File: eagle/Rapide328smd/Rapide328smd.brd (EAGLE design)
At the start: 50 x 50 mm, 34 parts, among them IC1 MEGA8-AI, J1 AVR_SPI_PRG_6PTH

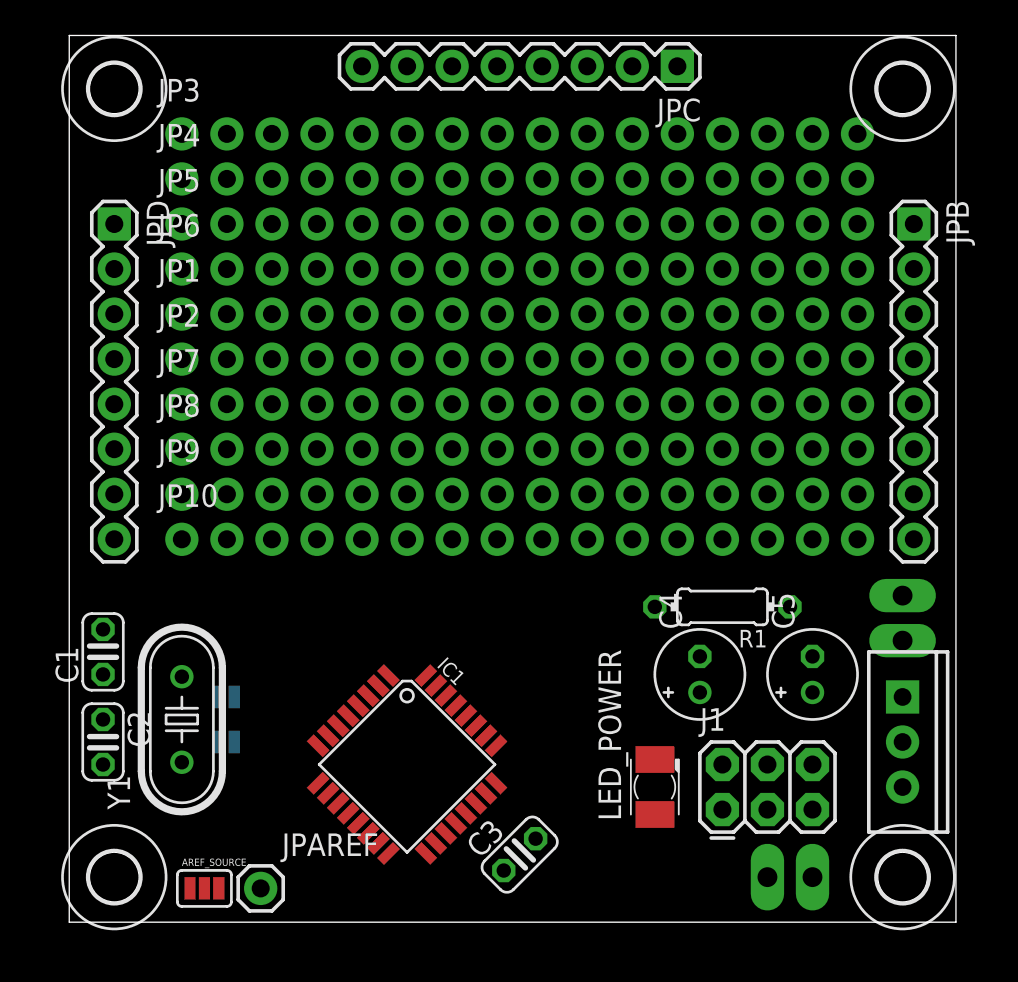
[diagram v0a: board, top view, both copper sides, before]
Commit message: Work in progress, started the wiring
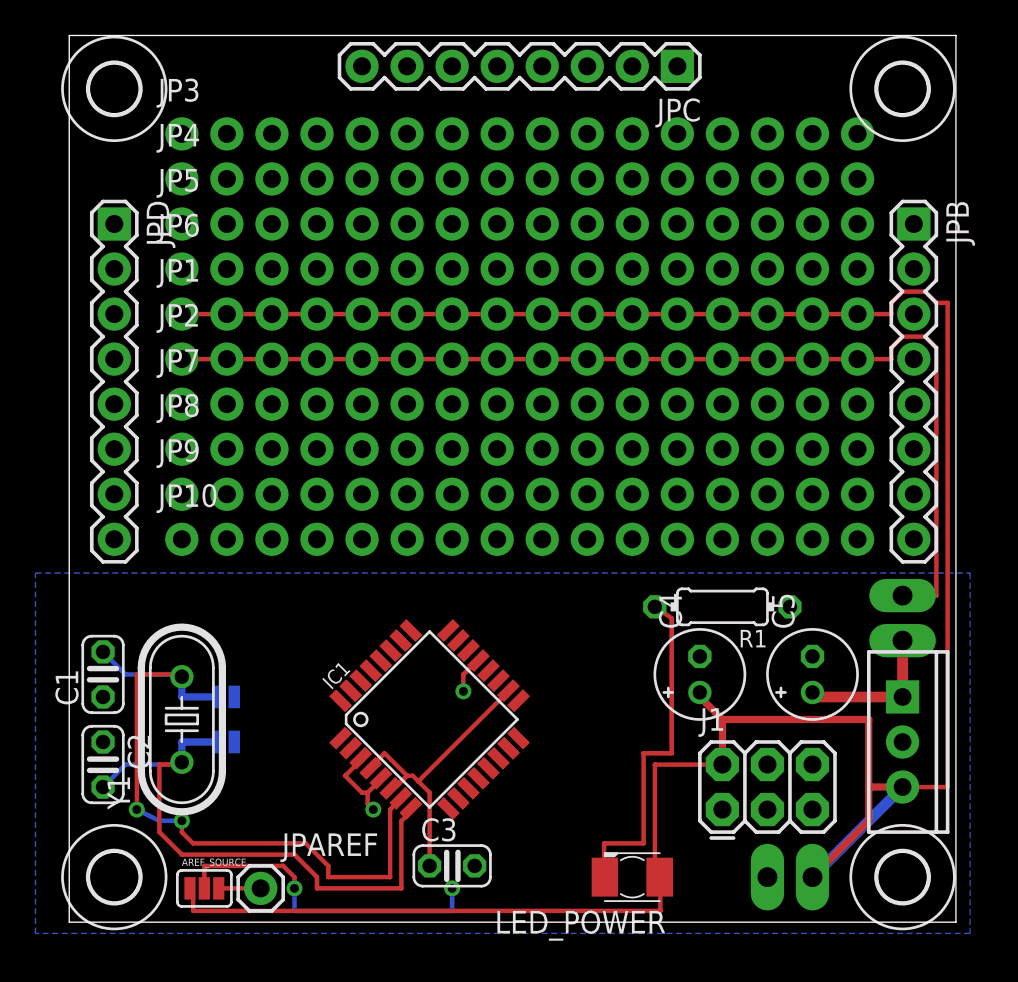
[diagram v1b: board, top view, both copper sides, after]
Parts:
- moved JP_RAW 17.6 mm to (47.0, 18.4), turned to 270 degrees
- moved JP_POWER 15.4 mm to (39.4, 2.54), turned to 0 degrees
- moved LED_POWER 5.24 mm to (31.8, 2.54), turned to 180 degrees
- moved C3 3.86 mm to (21.6, 3.17), turned to 0 degrees
- moved IC1 2.84 mm to (20.3, 11.4), turned to 45 degrees
- moved C1 1.27 mm to (1.91, 14.0)
- moved C2 1.27 mm to (1.91, 8.89)
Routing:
- net VCC: track 0.00 -> 133.1 mm
- net GND: track 0.00 -> 66.9 mm, vias 0 -> 2
- net N$25: track 0.00 -> 31.4 mm, vias 0 -> 2
- net N$34: track 0.00 -> 29.5 mm
- net N$2: track 0.00 -> 25.1 mm
- net N$30: track 0.00 -> 19.6 mm
- net N$3: track 0.00 -> 18.7 mm, vias 0 -> 2
- net VRAW: track 0.00 -> 8.39 mm
- net N$1: track 0.00 -> 8.28 mm
- net N$26: track 0.00 -> 8.15 mm
- net N$27: track 0.00 -> 2.22 mm
- added copper zone on layer 16, net GND

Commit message: Wiring continued. About 2/3 rd done.
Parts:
- moved C3 5.12 mm to (26.7, 2.54)
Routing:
- net N$14: track 0.00 -> 55.9 mm, vias 0 -> 1
- net N$12: track 0.00 -> 55.5 mm, vias 0 -> 1
- net N$28: track 0.00 -> 49.3 mm, vias 0 -> 3
- net N$32: track 0.00 -> 48.7 mm, vias 0 -> 2
- net N$36: track 0.00 -> 48.1 mm, vias 0 -> 3
- net RESET: track 0.00 -> 47.7 mm, vias 0 -> 3
- net N$7: track 0.00 -> 47.5 mm, vias 0 -> 1
- net N$17: track 0.00 -> 47.4 mm, vias 0 -> 1
- net N$16: track 0.00 -> 47.0 mm, vias 0 -> 1
- net N$15: track 0.00 -> 46.7 mm, vias 0 -> 1
- net N$11: track 0.00 -> 43.8 mm, vias 0 -> 1
- net VCC: track 133.1 -> 176.1 mm
- net N$9: track 0.00 -> 42.3 mm, vias 0 -> 1
- net N$44: track 0.00 -> 36.9 mm, vias 0 -> 1
- net N$40: track 0.00 -> 36.5 mm
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
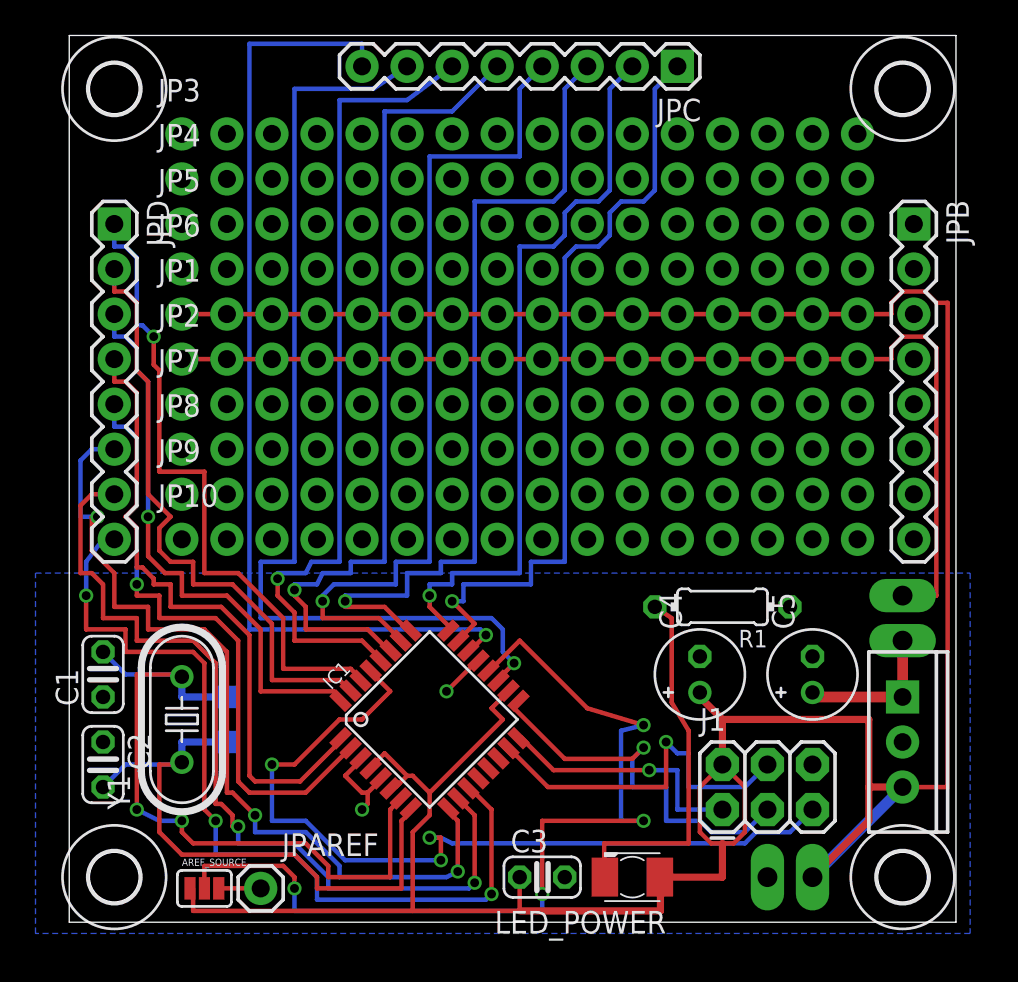
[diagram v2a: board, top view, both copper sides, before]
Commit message: Wiring done, must remove 2 useless solderpad switch
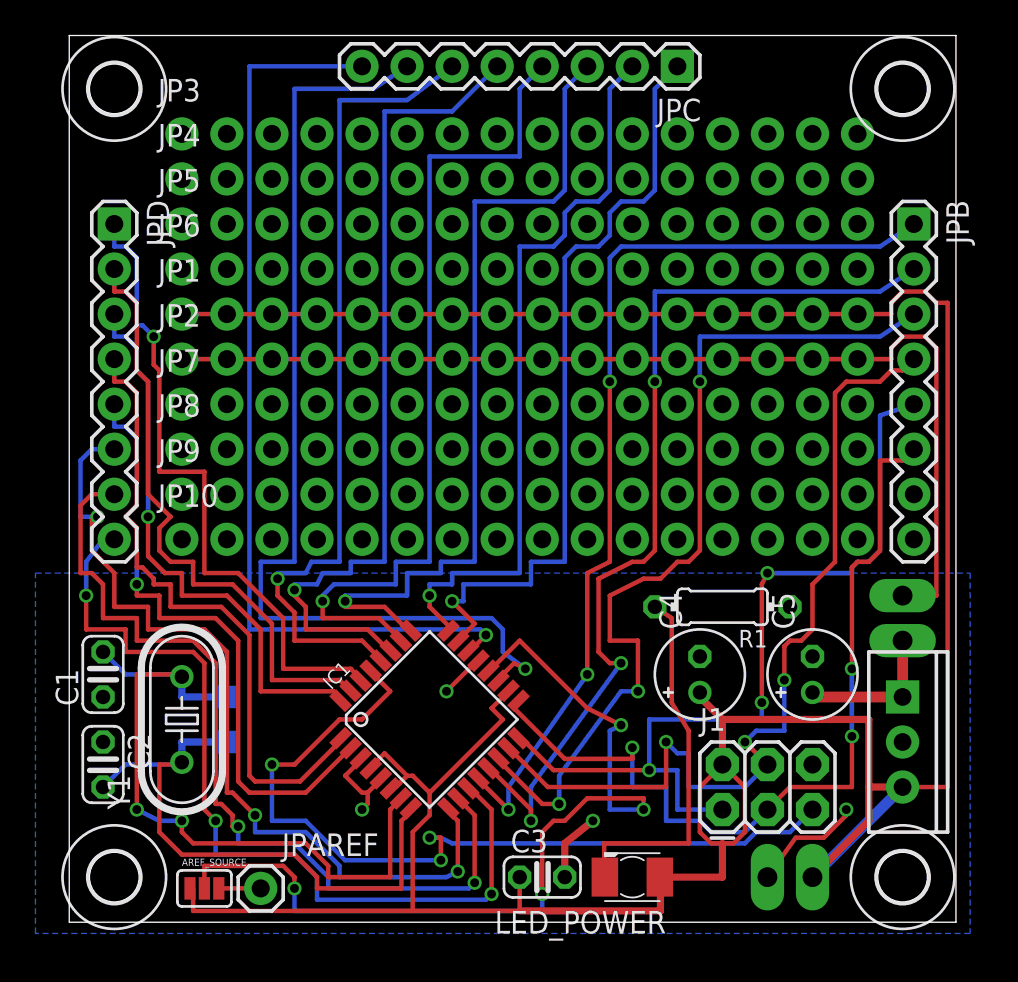
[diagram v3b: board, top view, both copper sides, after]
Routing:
- net N$13: track 0.00 -> 53.8 mm, vias 0 -> 3
- net N$34: track 0.00 -> 53.7 mm, vias 0 -> 3
- net N$38: track 0.00 -> 50.5 mm, vias 0 -> 3
- net MISO: track 14.4 -> 48.7 mm, vias 1 -> 3
- net MOSI: track 20.8 -> 50.9 mm, vias 1 -> 3
- net SCK: track 22.4 -> 48.8 mm, vias 1 -> 3
- net GND: track 67.3 -> 77.6 mm, vias 2 -> 4
- net N$12: track 55.5 -> 52.9 mm
- net N$14: track 55.9 -> 57.3 mm
- net N$18: track 52.3 -> 51.3 mm

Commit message: Wiring done, now labelling.
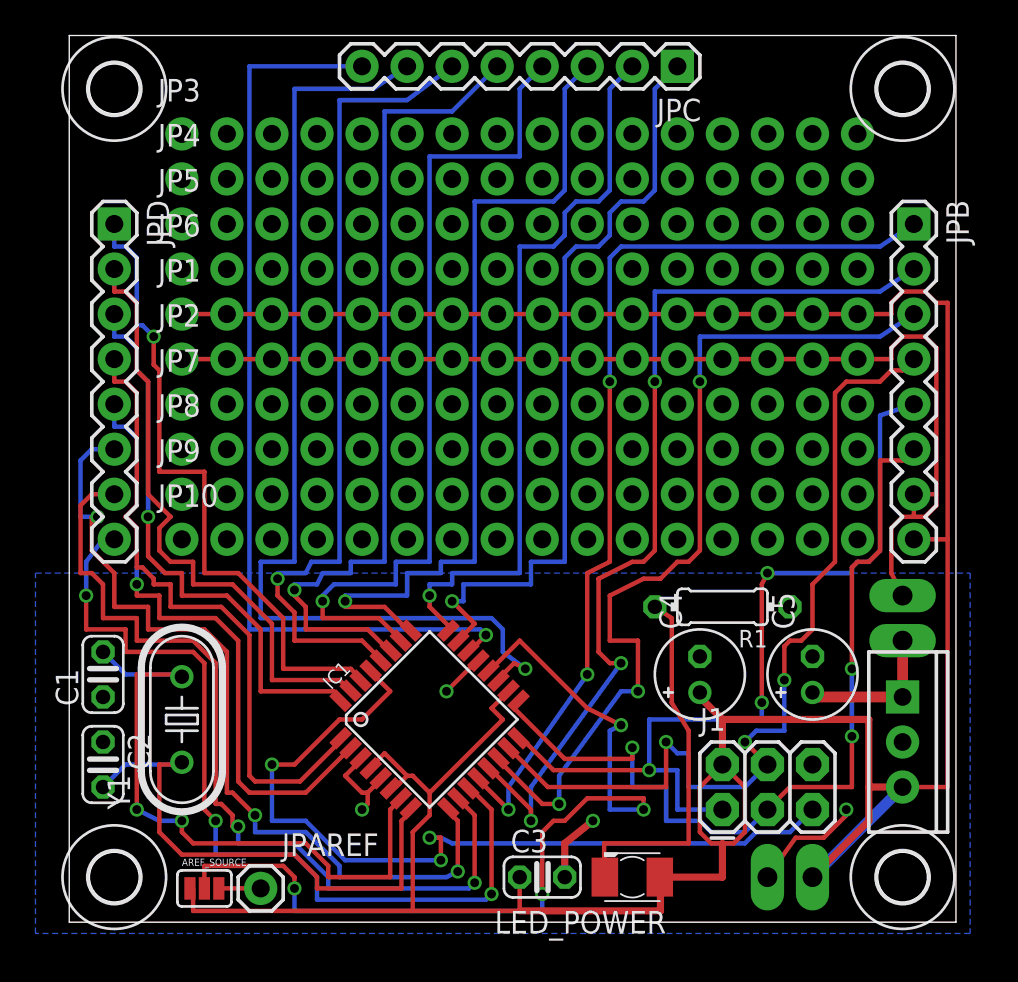
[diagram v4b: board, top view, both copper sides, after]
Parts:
- removed SJ1, SJ2: SOLDERJUMPERNC, SparkFun-Passives:SJ_2S
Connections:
- removed net N$23: JPB.7, SJ1.2
- removed net N$24: JPB.8, SJ2.2
- net GND: now also JPB.7
- net N$1: no longer SJ1.1
- net N$26: no longer SJ2.1
- net VCC: now also JPB.8
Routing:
- net N$1: track 8.28 -> 4.65 mm
- net N$26: track 8.15 -> 4.97 mm
- net GND: track 77.6 -> 80.2 mm
- net VCC: track 176.1 -> 178.0 mm
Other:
- board text added: "5V"
- board text added: "GND"
- board text added: "RAW"
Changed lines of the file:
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@@
 <layer number="35" name="tGlue" color="7" fill="4" visible="no" active="yes"/>
 <layer number="36" name="bGlue" color="7" fill="5" visible="no" active="yes"/>
-<layer number="37" name="tTest" color="7" fill="1" visible="no" active="yes"/>
+<layer number="37" name="tTest" color="7" fill="1" visible="yes" active="yes"/>
 <layer number="38" name="bTest" color="7" fill="1" visible="no" active="yes"/>
 <layer number="39" name="tKeepout" color="4" fill="11" visible="yes" active="yes"/>
@@
 <layer number="121" name="_tsilk" color="7" fill="1" visible="no" active="yes"/>
 <layer number="122" name="_bsilk" color="7" fill="1" visible="no" active="yes"/>
-<layer number="125" name="_tNames" color="7" fill="1" visible="no" active="yes"/>
+<layer number="125" name="_tNames" color="7" fill="1" visible="yes" active="yes"/>
 <layer number="144" name="Drill_legend" color="7" fill="1" visible="no" active="yes"/>
 <layer number="151" name="HeatSink" color="7" fill="1" visible="no" active="yes"/>
@@
 <wire x1="50" y1="50" x2="0" y2="50" width="0" layer="20"/>
 <wire x1="0" y1="50" x2="0" y2="0" width="0" layer="20"/>
+<wire x1="46.99" y1="25.4" x2="48.26" y2="25.4" width="0.254" layer="125"/>
+<wire x1="46.99" y1="22.86" x2="48.26" y2="22.86" width="0.254" layer="125"/>
+<wire x1="46.355" y1="25.4" x2="48.895" y2="25.4" width="0.254" layer="125"/>
+<wire x1="48.895" y1="25.4" x2="48.895" y2="20.32" width="0.254" layer="125"/>
+<wire x1="48.895" y1="20.32" x2="46.355" y2="20.32" width="0.254" layer="125"/>
+<wire x1="46.355" y1="20.32" x2="46.355" y2="25.4" width="0.254" layer="125"/>
+<wire x1="29.21" y1="3.81" x2="30.48" y2="3.81" width="0.4064" layer="125"/>
+<wire x1="30.48" y1="3.81" x2="29.21" y2="2.54" width="0.4064" layer="125"/>
+<wire x1="29.21" y1="2.54" x2="29.21" y2="3.81" width="0.4064" layer="125"/>
+<text x="34.925" y="0.635" size="1.27" layer="125">GND</text>
+<text x="43.18" y="3.175" size="1.27" layer="125">5V</text>
+<text x="41.91" y="18.415" size="1.27" layer="125">GND</text>
+<text x="41.91" y="15.875" size="1.27" layer="125">RAW</text>
 </plain>
 <attributes>
@@
 <element name="JPD" library="SparkFun-Connectors" package="1X08" value="" x="2.54" y="39.37" rot="R270"/>
 <element name="JPB" library="SparkFun-Connectors" package="1X08" value="" x="47.625" y="39.37" rot="R270"/>
-<element name="SJ1" library="SparkFun-Passives" package="SJ_2S" value="SOLDERJUMPERNC" x="8.89" y="12.7" rot="MR0"/>
-<element name="SJ2" library="SparkFun-Passives" package="SJ_2S" value="SOLDERJUMPERNC" x="8.89" y="10.16" rot="MR180"/>
 <element name="JP1" library="SparkFun-Connectors" package="1X16_NO_SILK" value="M161X16_NO_SILK" x="6.35" y="34.29"/>
 <element name="JP2" library="SparkFun-Connectors" package="1X16_NO_SILK" value="M161X16_NO_SILK" x="6.35" y="31.75"/>
@@
 <vertex x="-1.905" y="-0.635"/>
 </polygon>
-<wire x1="46.99" y1="18.415" x2="48.895" y2="18.415" width="0.254" layer="1"/>
-<wire x1="48.895" y1="18.415" x2="48.895" y2="32.385" width="0.254" layer="1"/>
+<wire x1="46.99" y1="18.415" x2="46.355" y2="19.685" width="0.254" layer="1"/>
+<wire x1="46.355" y1="19.685" x2="46.355" y2="22.225" width="0.254" layer="1"/>
+<wire x1="46.355" y1="22.225" x2="46.99" y2="22.86" width="0.254" layer="1"/>
+<wire x1="46.99" y1="22.86" x2="47.625" y2="22.86" width="0.254" layer="1"/>
+<wire x1="47.625" y1="22.86" x2="48.26" y2="22.86" width="0.254" layer="1"/>
+<wire x1="48.26" y1="22.86" x2="48.895" y2="23.495" width="0.254" layer="1"/>
+<wire x1="48.895" y1="23.495" x2="48.895" y2="24.13" width="0.254" layer="1"/>
+<wire x1="48.895" y1="24.13" x2="48.895" y2="32.385" width="0.254" layer="1"/>
 <wire x1="48.895" y1="32.385" x2="48.26" y2="33.02" width="0.254" layer="1"/>
 <wire x1="48.26" y1="33.02" x2="46.99" y2="33.02" width="0.254" layer="1"/>
@@
 <via x="43.815" y="6.35" extent="1-16" drill="0.5"/>
 <wire x1="43.815" y1="6.0325" x2="43.815" y2="6.35" width="0.254" layer="1"/>
+<contactref element="JPB" pad="7"/>
+<wire x1="47.625" y1="22.86" x2="47.625" y2="24.13" width="0.254" layer="1"/>
+<wire x1="47.625" y1="24.13" x2="48.895" y2="24.13" width="0.254" layer="1"/>
 <wire x1="22.86" y1="14.605" x2="23.07248125" y2="14.74816875" width="0" layer="19" extent="1-1"/>
 <wire x1="16.43614375" y1="9.2432" x2="16.51" y2="9.2075" width="0" layer="19" extent="1-1"/>
@@
 <wire x1="48.26" y1="35.56" x2="48.895" y2="34.925" width="0.254" layer="1"/>
 <wire x1="48.895" y1="34.925" x2="49.53" y2="34.925" width="0.254" layer="1"/>
-<wire x1="49.53" y1="34.925" x2="49.53" y2="7.62" width="0.254" layer="1"/>
+<wire x1="49.53" y1="34.925" x2="49.53" y2="21.59" width="0.254" layer="1"/>
+<wire x1="49.53" y1="21.59" x2="49.53" y2="7.62" width="0.254" layer="1"/>
 <wire x1="49.53" y1="7.62" x2="46.99" y2="7.62" width="0.254" layer="1"/>
 <wire x1="36.83" y1="8.89" x2="38.1" y2="7.62" width="0.254" layer="1"/>
@@
 <wire x1="25.4" y1="0.635" x2="25.4" y2="2.54" width="0.254" layer="1"/>
 <wire x1="6.985" y1="0.635" x2="19.3675" y2="0.635" width="0.254" layer="1"/>
-<wire x1="20.32" y1="0.635" x2="20.955" y2="0.635" width="0.254" layer="1"/>
-<wire x1="20.955" y1="0.635" x2="25.4" y2="0.635" width="0.254" layer="1"/>
+<wire x1="19.3675" y1="0.635" x2="25.4" y2="0.635" width="0.254" layer="1"/>
 <wire x1="25.4" y1="0.635" x2="33.3375" y2="0.635" width="0.4064" layer="1"/>
 <wire x1="33.3375" y1="0.635" x2="33.3375" y2="2.2225" width="0.4064" layer="1"/>
@@
 <wire x1="35.56" y1="5.08" x2="36.195" y2="4.445" width="0.254" layer="1"/>
 <wire x1="36.195" y1="4.445" x2="36.83" y2="4.445" width="0.254" layer="1"/>
-<wire x1="19.3675" y1="0.635" x2="20.32" y2="0.635" width="0.254" layer="1"/>
+<contactref element="JPB" pad="8"/>
+<wire x1="49.53" y1="21.59" x2="47.625" y2="21.59" width="0.254" layer="1"/>
 <wire x1="35.56" y1="13.0175" x2="35.56" y2="12.954" width="0" layer="19" extent="1-1"/>
 <wire x1="24.7695375" y1="13.0511125" x2="24.765" y2="13.0175" width="0" layer="19" extent="1-1"/>
@@
 <contactref element="Y1" pad="2"/>
 <contactref element="IC1" pad="7"/>
-<contactref element="SJ1" pad="1"/>
 <wire x1="1.905" y1="15.24" x2="3.175" y2="13.97" width="0.254" layer="16"/>
-<wire x1="6.35" y1="13.97" x2="6.35" y2="13.6525" width="0.4064" layer="16"/>
-<wire x1="6.35" y1="13.6525" x2="6.35" y2="12.7" width="0.4064" layer="16"/>
-<wire x1="6.35" y1="12.7" x2="8.255" y2="12.7" width="0.4064" layer="16"/>
 <wire x1="3.175" y1="13.97" x2="6.0325" y2="13.97" width="0.254" layer="16"/>
-<wire x1="6.0325" y1="13.97" x2="6.35" y2="13.6525" width="0.254" layer="16"/>
-<wire x1="9.3019" y1="12.7" x2="18.698884375" y2="6.980459375" width="0" layer="19" extent="1-16"/>
-<wire x1="8.255" y1="12.7" x2="9.3019" y2="12.7" width="0" layer="19" extent="16-16"/>
-<wire x1="6.35" y1="13.843" x2="6.35" y2="13.97" width="0" layer="19" extent="16-16"/>
+<wire x1="6.35" y1="13.843" x2="18.698884375" y2="6.980459375" width="0" layer="19" extent="1-1"/>
+<wire x1="6.0325" y1="13.97" x2="6.35" y2="13.843" width="0" layer="19" extent="16-16"/>
 </signal>
 <signal name="MISO">
@@
 <wire x1="24.765" y1="9.8425" x2="24.7695375" y2="9.808884375" width="0" layer="19" extent="1-1"/>
 </signal>
-<signal name="N$23">
-<contactref element="SJ1" pad="2"/>
-<contactref element="JPB" pad="7"/>
-<wire x1="8.4781" y1="12.7" x2="47.625" y2="24.13" width="0" layer="19" extent="16-16"/>
-</signal>
-<signal name="N$24">
-<contactref element="JPB" pad="8"/>
-<contactref element="SJ2" pad="2"/>
-<wire x1="9.3019" y1="10.16" x2="47.625" y2="21.59" width="0" layer="19" extent="16-16"/>
-</signal>
 <signal name="N$27">
 <contactref element="AREF_SOURCE" pad="3"/>
@@
 <contactref element="Y1" pad="1"/>
 <contactref element="C2" pad="2"/>
-<contactref element="SJ2" pad="1"/>
 <wire x1="1.905" y1="7.62" x2="3.175" y2="8.89" width="0.254" layer="16"/>
-<wire x1="6.35" y1="8.89" x2="6.35" y2="10.16" width="0.4064" layer="16"/>
-<wire x1="6.35" y1="10.16" x2="8.255" y2="10.16" width="0.4064" layer="16"/>
 <wire x1="3.175" y1="8.89" x2="6.35" y2="8.89" width="0.254" layer="16"/>
-<wire x1="8.4781" y1="10.16" x2="19.264571875" y2="6.414771875" width="0" layer="19" extent="1-16"/>
-<wire x1="8.255" y1="10.16" x2="8.4781" y2="10.16" width="0" layer="19" extent="16-16"/>
+<wire x1="6.35" y1="8.89" x2="19.264571875" y2="6.414771875" width="0" layer="19" extent="1-16"/>
 <wire x1="6.35" y1="9.017" x2="6.35" y2="8.89" width="0" layer="19" extent="16-16"/>
 </signal>
@@
 <wire x1="5.08" y1="5.08" x2="5.08" y2="8.89" width="0.254" layer="1"/>
 <wire x1="5.08" y1="8.89" x2="6.35" y2="8.89" width="0.254" layer="1"/>
+<wire x1="6.35" y1="8.89" x2="6.35" y2="9.2075" width="0.254" layer="1"/>
 </signal>
 <signal name="N$25">
@@
 <wire x1="3.81" y1="6.35" x2="3.81" y2="13.97" width="0.254" layer="1"/>
 <wire x1="3.81" y1="13.97" x2="6.35" y2="13.97" width="0.254" layer="1"/>
+<wire x1="6.35" y1="13.97" x2="6.35" y2="13.6525" width="0.254" layer="1"/>
 </signal>
 <signal name="N$28">

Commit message: Version 1.0 finished, ready to go to production
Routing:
- net GND: track 80.2 -> 92.1 mm, vias 4 -> 6
- net RESET: track 47.7 -> 47.1 mm
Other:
- board text added: "+"
- board text added: "-"
- board text added: "10"
- board text added: "100"
- board text added: "1uF"
- board text added: "AREF"
- board text added: "ATmega 328-AU"
- board text added: "B0"
- board text added: "C0"
- board text added: "D0"
- board text added: "LED"
- board text added: "LM7805"
- board text added: "Power"
- board text added: "Ver 1.0 Dec2012"
- board text added: "http://kalshagar.wikispaces.com/Rapide328smd"
